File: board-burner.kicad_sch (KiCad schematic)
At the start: 18 parts, among them J2 TH1, J3 FAN, J4 Conn_WallSocket_Earth, J5 Conn_WallSocket_Earth, J7 Conn_WallSocket_Earth, Q1 2N7000, Q2 Q_NMOS_DGS, Q3 Q_PMOS_DGS, SW1 PWR

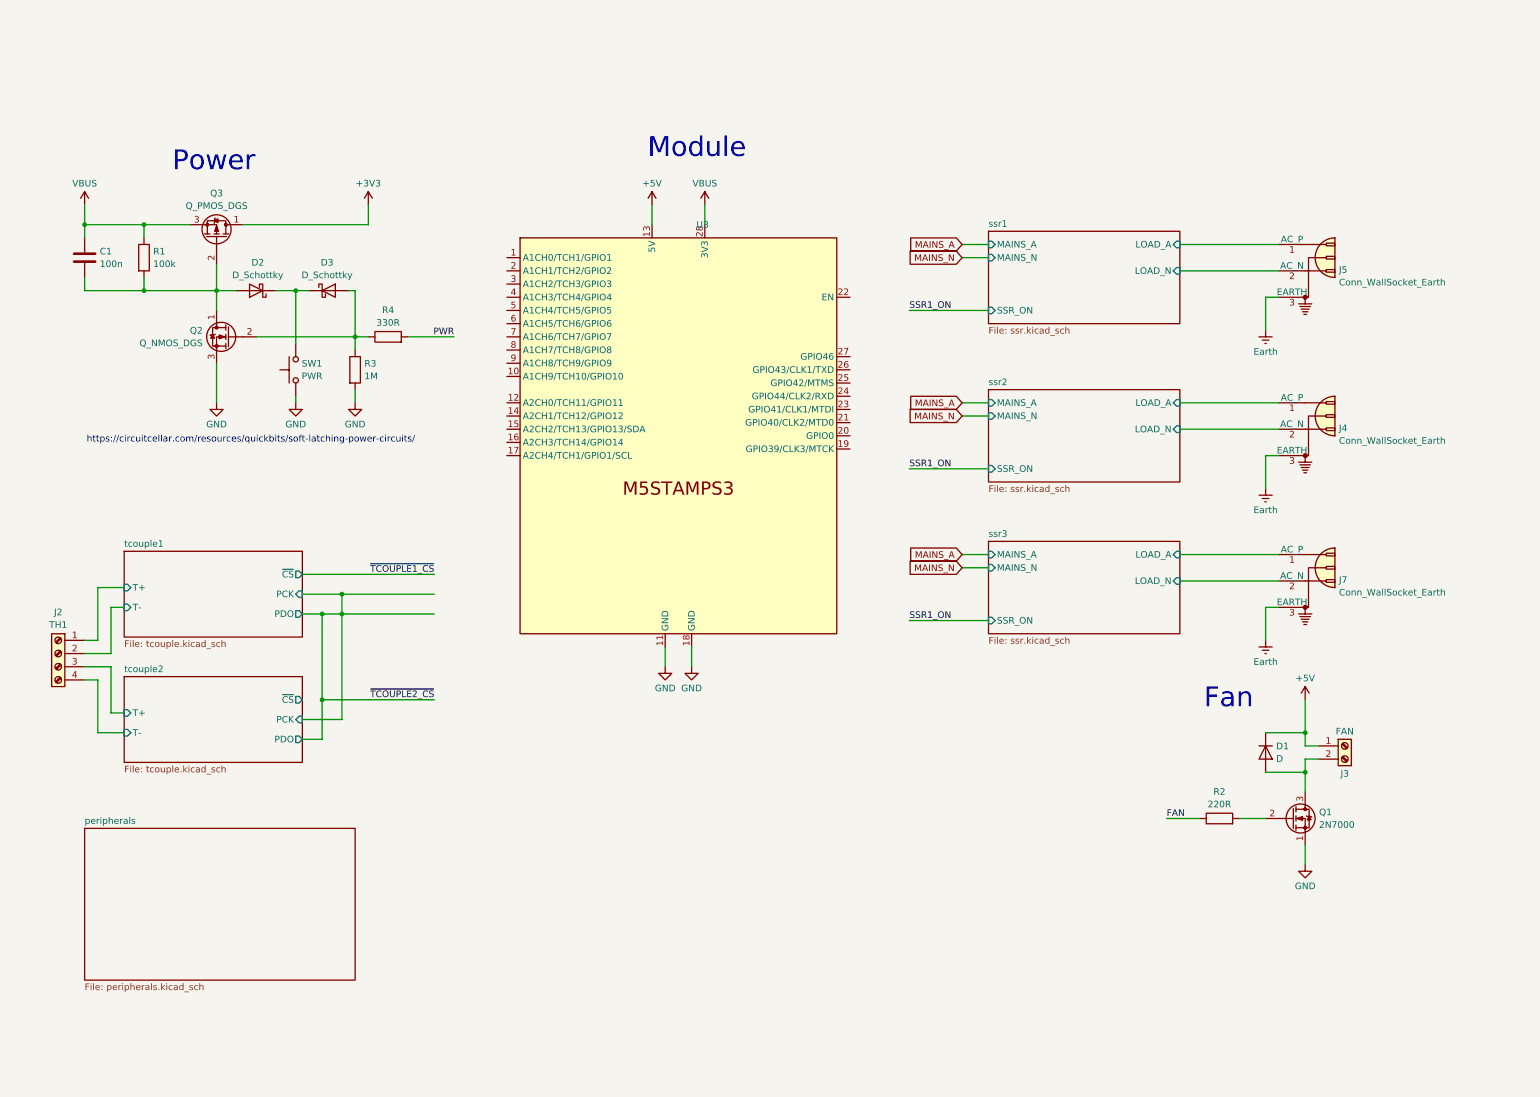
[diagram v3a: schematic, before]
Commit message: Further work, most components now present
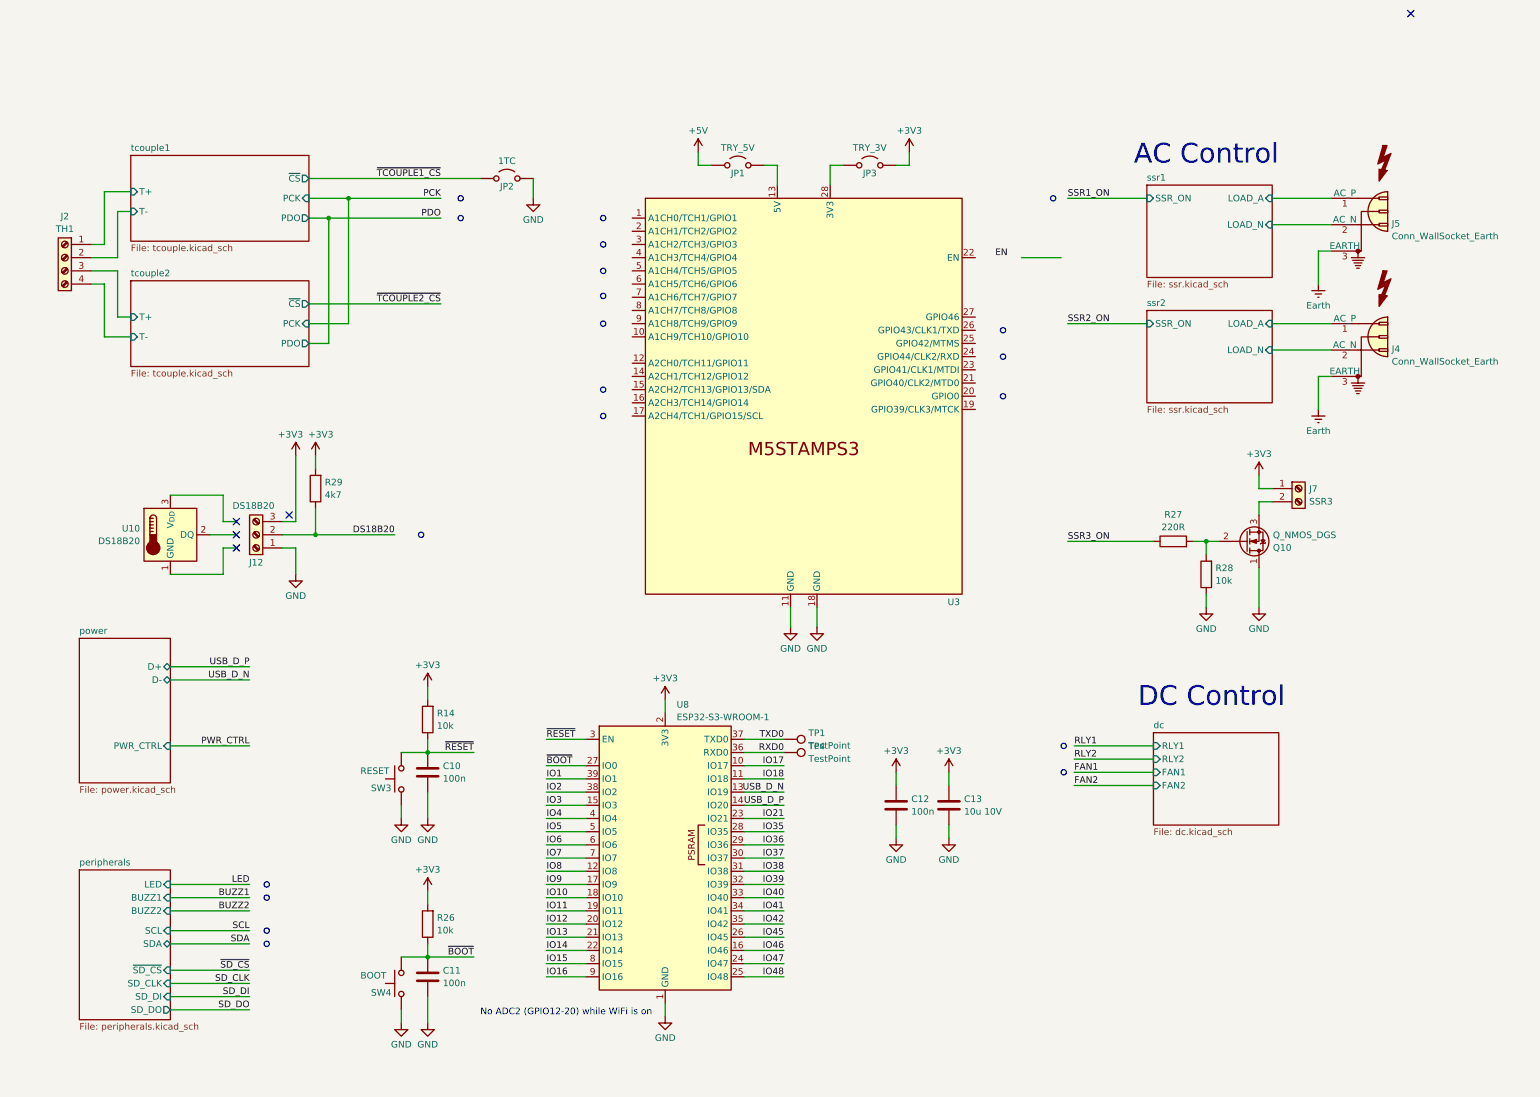
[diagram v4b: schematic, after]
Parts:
- removed C1: 100n, symbol Device:C
- removed D1: D, symbol Device:D
- removed D2, D3: D_Schottky, symbol Device:D_Schottky
- removed J3: FAN, symbol Connector:Screw_Terminal_01x02
- removed J7: Conn_WallSocket_Earth, symbol Connector:Conn_WallSocket_Earth
- removed Q1: 2N7000, Package_TO_SOT_THT:TO-92_Inline, symbol Transistor_FET:2N7000
- removed Q2: Q_NMOS_DGS, symbol Device:Q_NMOS_DGS
- removed Q3: Q_PMOS_DGS, symbol Device:Q_PMOS_DGS
- removed R1: 100k, symbol Device:R
- removed R2: 220R, symbol Device:R
- removed R3: 1M, symbol Device:R
- removed R4: 330R, symbol Device:R
- removed SW1: PWR, symbol Switch:SW_Push
- added C10, C11, C12: 100n, symbol Device:C
- added C13: 10u 10V, symbol Device:C
- added J12: DS18B20, symbol Connector:Screw_Terminal_01x03
- added J7: SSR3, symbol Connector:Screw_Terminal_01x02
- added JP1: TRY_5V, symbol Jumper:Jumper_2_Open
- added JP2: 1TC, symbol Jumper:Jumper_2_Open
- added JP3: TRY_3V, symbol Jumper:Jumper_2_Open
- added Q10: Q_NMOS_DGS, symbol Device:Q_NMOS_DGS
- added R14, R26, R28: 10k, symbol Device:R
- added R27: 220R, symbol Device:R
- added R29: 4k7, symbol Device:R
- added SW3: RESET, symbol Switch:SW_Push
- added SW4: BOOT, symbol Switch:SW_Push
- added TP1, TP4: TestPoint, symbol Connector:TestPoint
- added U10: DS18B20, Package_TO_SOT_THT:TO-92_Inline, symbol Sensor_Temperature:DS18B20
- added U8: ESP32-S3-WROOM-1, RF_Module:ESP32-S3-WROOM-1, symbol RF_Module:ESP32-S3-WROOM-1
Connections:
- net +3V3: now also C12.1, C13.1, J12.3 (Pin_3), J7.1 (Pin_1), JP3.2 (B), R14.2, R26.2, R29.2, U8.2 (3V3)
- net +5V: now also JP1.1 (A); no longer U3.13 (5V)
- net GND: now also C10.2, C11.2, C12.2, C13.2, J12.1 (Pin_1), JP2.2 (B), Q10.1 (D), R28.1, SW3.1, SW4.1, U8.1 (GND), U8.40 (GND), U8.41 (GND)
- net ~{TCOUPLE1_CS}: now also JP2.1 (A)
- net VBUS: no longer names the net of U3.28 (3V3)
- net VBUS: now also JP3.1 (A)
- new net: JP1.2 (B), U3.13 (5V)
- new net: Q10.2 (G), R27.2, R28.2
- new net: J7.2 (Pin_2), Q10.3 (S)
- new net DS18B20: J12.2 (Pin_2), R29.1
- new net IO1: U8.39 (IO1)
- new net IO10: U8.18 (IO10)
- new net IO11: U8.19 (IO11)
- new net IO12: U8.20 (IO12)
- new net IO13: U8.21 (IO13)
- new net IO14: U8.22 (IO14)
- new net IO15: U8.8 (IO15)
- new net IO16: U8.9 (IO16)
- new net IO17: U8.10 (IO17)
- new net IO18: U8.11 (IO18)
- new net IO2: U8.38 (IO2)
- new net IO21: U8.23 (IO21)
- new net IO3: U8.15 (IO3)
- new net IO35: U8.28 (IO35)
- new net IO36: U8.29 (IO36)
- new net IO37: U8.30 (IO37)
- new net IO38: U8.31 (IO38)
- new net IO39: U8.32 (IO39)
- new net IO4: U8.4 (IO4)
- new net IO40: U8.33 (IO40)
- new net IO41: U8.34 (IO41)
- new net IO42: U8.35 (IO42)
- new net IO45: U8.26 (IO45)
- new net IO46: U8.16 (IO46)
- new net IO47: U8.24 (IO47)
- new net IO48: U8.25 (IO48)
- new net IO5: U8.5 (IO5)
- new net IO6: U8.6 (IO6)
- new net IO7: U8.7 (IO7)
- new net IO8: U8.12 (IO8)
- new net IO9: U8.17 (IO9)
- new net RXD0: TP4.1, U8.36 (RXD0)
- new net SSR3_ON: R27.1
- new net TXD0: TP1.1, U8.37 (TXD0)
- new net USB_D_N: U8.13 (IO19)
- new net USB_D_P: U8.14 (IO20)
- new net ~{BOOT}: C11.1, R26.1, SW4.2, U8.27 (IO0)
- new net ~{RESET}: C10.1, R14.1, SW3.2, U8.3 (EN)
- no-connect marks 0 -> 5
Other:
- removed sheet ssr3
- added sheet dc (dc.kicad_sch)
- added sheet power (power.kicad_sch)
- sheet peripherals ports: added BUZZ1, BUZZ2, LED, SCL, SDA, SD_CLK, SD_DI, SD_DO, ~{SD_CS}; removed none
- sheet ssr1 ports: added none; removed MAINS_A, MAINS_N
- sheet ssr2 ports: added none; removed MAINS_A, MAINS_N
- note added: "AC Control"
- note added: "DC Control"
- note added: "No ADC2 (GPIO12-20) while WiFi is on"
- note removed: "Fan"
- note removed: "Module"
- note removed: "Power"
- note removed: "https://circuitcellar.com/resources/quickbits/soft-latching-power-circuits/"
- moved on the sheet: J2, J4, J5, U3
